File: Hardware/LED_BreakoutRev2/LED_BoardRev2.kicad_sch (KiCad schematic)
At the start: 39 parts

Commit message: First draft of LED board Schematic
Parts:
- added Conn?: Molex_SL_08, symbol MRDT_Connectors:Molex_SL_08
- added D? (x2): 365nm, symbol Device:LED
- added D? (x2): 265nm, symbol Device:LED
- added D? (x2): 275nm, symbol Device:LED
- added D? (x2): 310nm, symbol Device:LED
- added D?: LED, symbol Device:LED
- added D? (x2): 285nm, symbol Device:LED
- added Q? (x6): BSS214NW, Package_TO_SOT_SMD:SOT-323_SC-70, symbol Transistor_FET:BSS214NW
- added R? (x11): R, symbol Device:R
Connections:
- net +12V: now also Conn?.7, D?.2 (A), D?.2 (A), D?.2 (A), D?.2 (A), D?.2 (A), D?.2 (A), D?.2 (A), D?.2 (A), D?.2 (A), D?.2 (A), D?.2 (A)
- net GND: now also Conn?.8, Q?.2 (S), Q?.2 (S), Q?.2 (S), Q?.2 (S), Q?.2 (S), Q?.2 (S)
- new net: Conn?.2, Q?.1 (G)
- new net: Q?.3 (D), R?.2, R?.2 (x5)
- new net: Conn?.5, Q?.1 (G)
- new net: D?.1 (K), R?.1 (x11)
- new net: Q?.3 (D), R?.2
- new net: Conn?.1, Q?.1 (G)
- new net: Conn?.4, Q?.1 (G)
- new net: Conn?.3, Q?.1 (G)
- new net: Conn?.6, Q?.1 (G)
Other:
- moved on the sheet: Conn?, D?, Q?, R?, V?

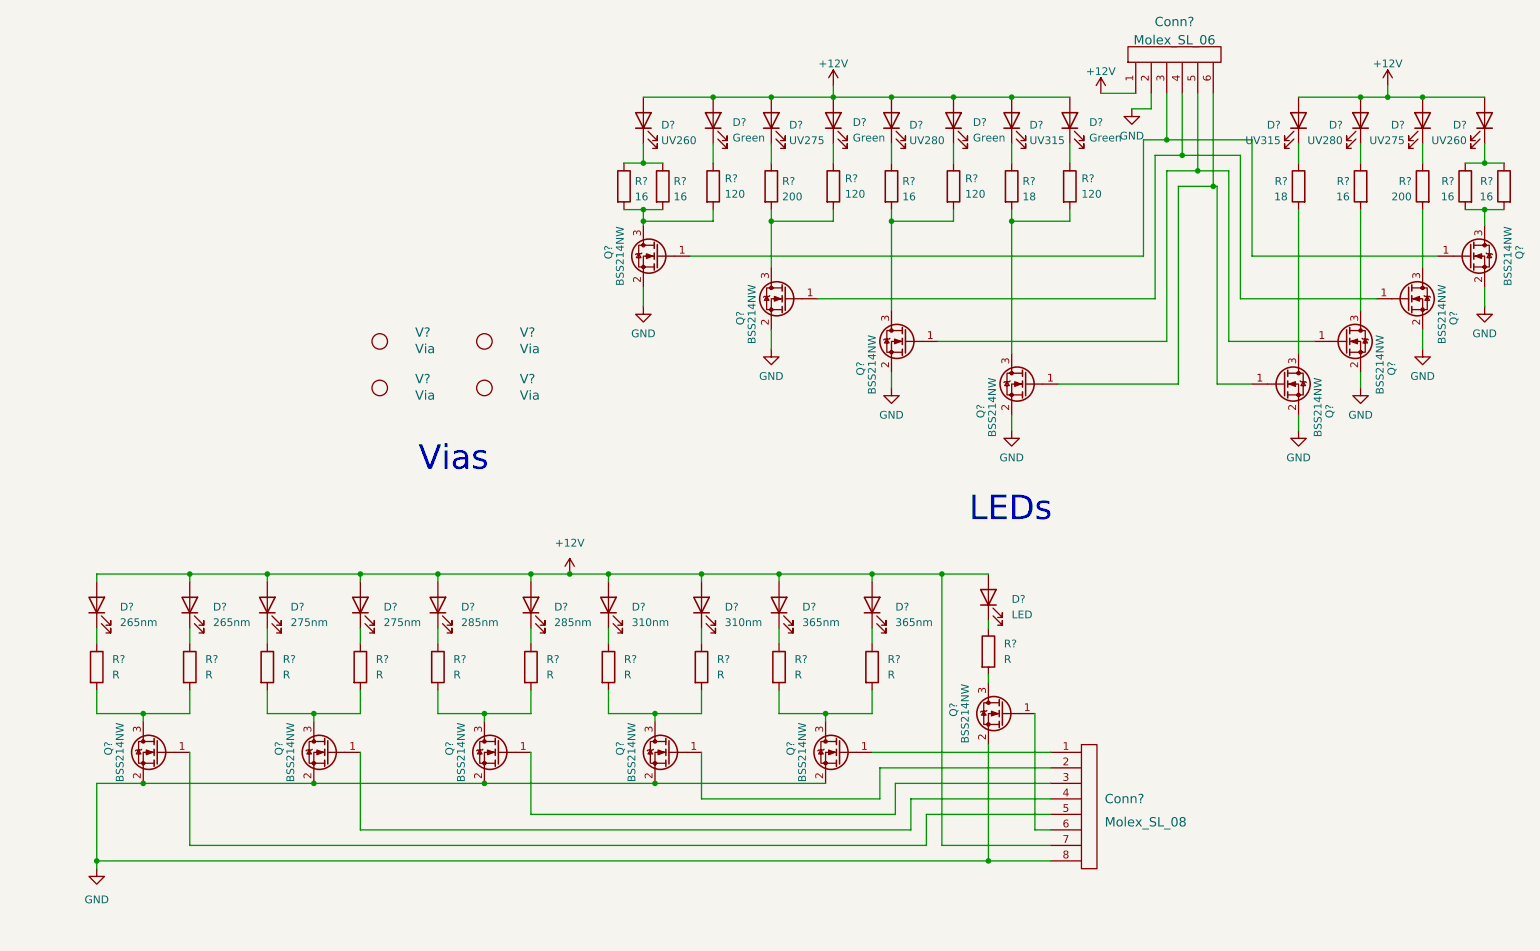
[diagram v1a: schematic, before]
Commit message: LED footprints
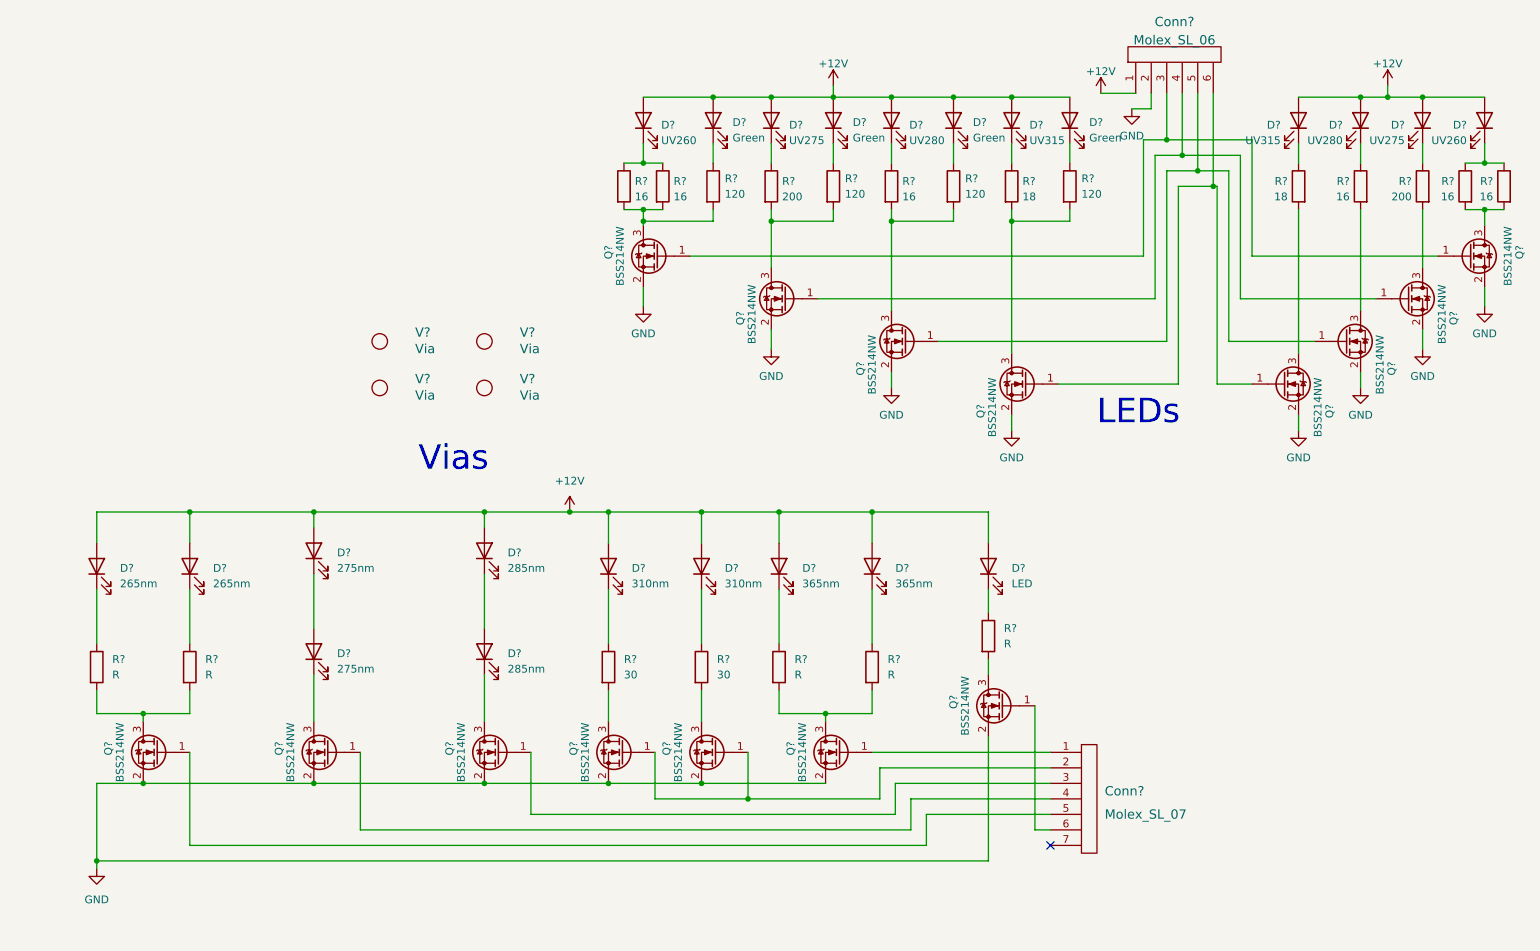
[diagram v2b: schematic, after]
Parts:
- removed Conn?: Molex_SL_08, symbol MRDT_Connectors:Molex_SL_08
- removed D? (x2): 265nm, symbol Device:LED
- removed D?: 275nm, symbol Device:LED
- removed R? (x5): R, symbol Device:R
- added Conn?: Molex_SL_07, symbol MRDT_Connectors:Molex_SL_07
- added D? (x2): 265nm, KL265-50W-SM-WD Footprint:3535, symbol Device:LED
- added D?: 275nm, symbol Device:LED
- added Q?: BSS214NW, Package_TO_SOT_SMD:SOT-323_SC-70, symbol Transistor_FET:BSS214NW
- added R?: 30, symbol Device:R
- R?: value R -> 30
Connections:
- net +12V: now also D?.2 (A), D?.2 (A), D?.2 (A); no longer D?.2 (A), D?.2 (A)
- net GND: now also Q?.2 (S)
- net at Q?.1 (G): now also Conn?.2, Q?.1 (G)
- net at Q?.3 (D): now also R?.2; no longer R?.2
- net at Q?.1 (G): now also Conn?.5
- net at D?.1 (K): now also R?.1
- net at D?.1 (K): now also Q?.3 (D) (x2)
- net at R?.1: now also D?.1 (K) (x2)
- net at Q?.1 (G): now also Conn?.1
- net at D?.1 (K): now also D?.2 (A)
- net at Q?.1 (G): now also Conn?.4
- net at Q?.1 (G): now also Conn?.3
- net at Q?.1 (G): now also Conn?.6
- new net: Q?.3 (D), R?.2
- new net: D?.1 (K), D?.2 (A)
- no-connect marks 0 -> 1
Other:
- moved on the sheet: D?, Q?, R?

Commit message: Added resistor values and LED datasheets
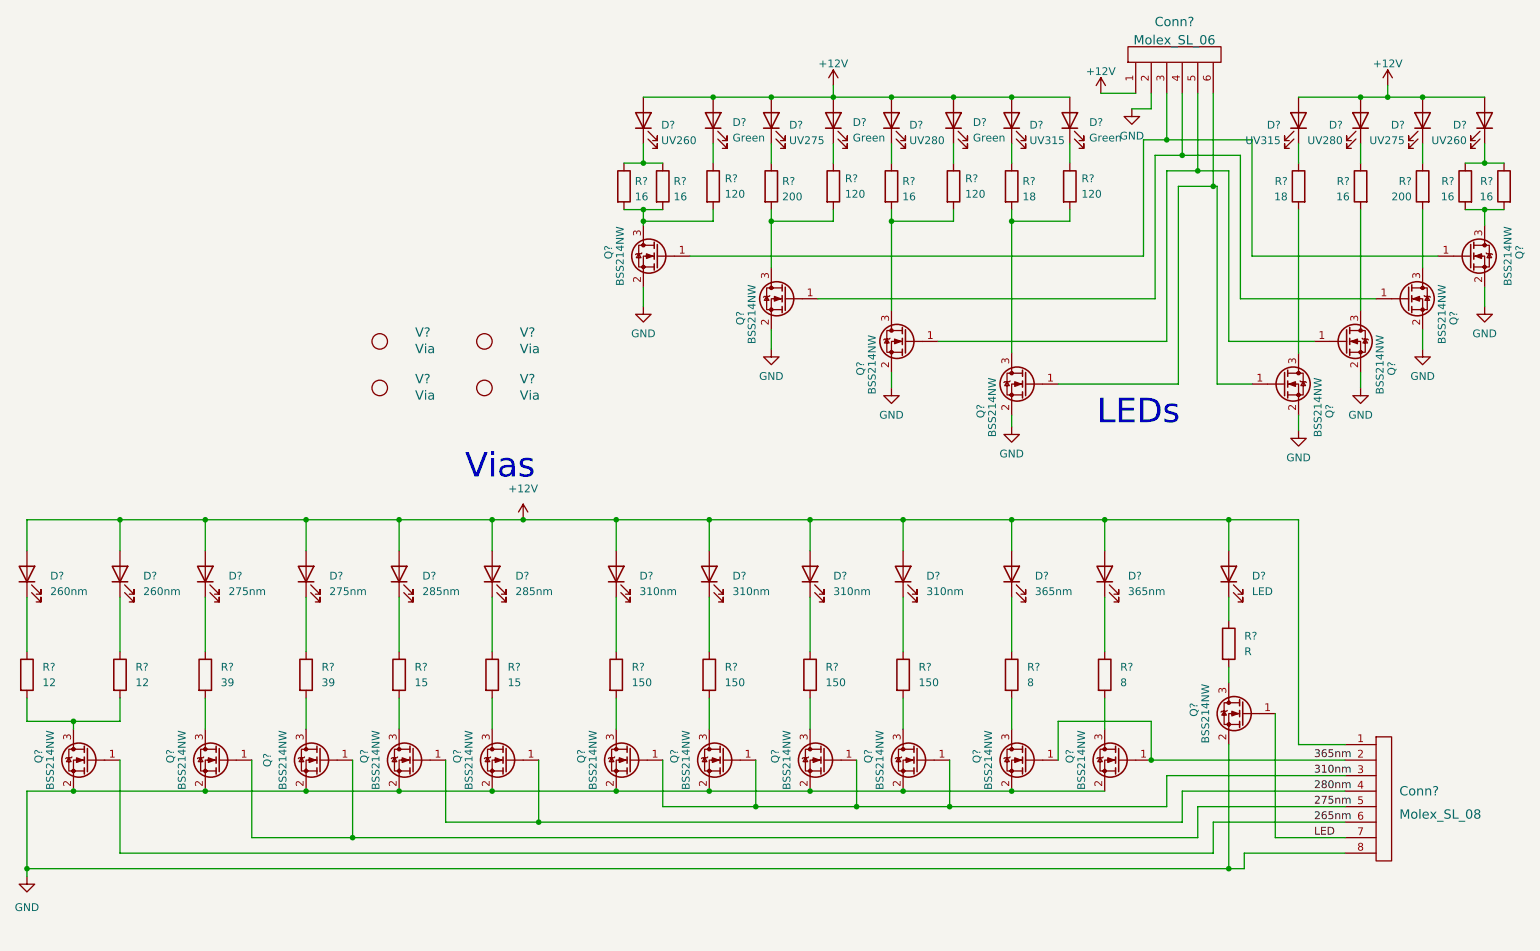
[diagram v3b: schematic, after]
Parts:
- removed Conn?: Molex_SL_07, symbol MRDT_Connectors:Molex_SL_07
- removed D?: 265nm, KL265-50W-SM-WD Footprint:3535, symbol Device:LED
- removed D?: 275nm, symbol Device:LED
- removed D?: 285nm, symbol Device:LED
- removed D?: 365nm, symbol Device:LED
- removed D?: 310nm, symbol Device:LED
- removed R? (x2): R, symbol Device:R
- removed R?: 30, symbol Device:R
- added Conn?: Molex_SL_08, symbol MRDT_Connectors:Molex_SL_08
- added D? (x3): 310nm, symbol Device:LED
- added D?: 260nm, KL265-50W-SM-WD Footprint:3535, symbol Device:LED
- added D?: 365nm, symbol Device:LED
- added D?: 285nm, symbol Device:LED
- added D?: 275nm, symbol Device:LED
- added Q? (x5): BSS214NW, Package_TO_SOT_SMD:SOT-323_SC-70, symbol Transistor_FET:BSS214NW
- added R?: 12, symbol Device:R
- added R? (x3): 150, symbol Device:R
- added R?: 8, symbol Device:R
- added R? (x2): 15, symbol Device:R
- added R? (x2): 39, symbol Device:R
- D?: value 265nm -> 260nm
- R?: value 30 -> 150
- R?: value R -> 12
- R?: value R -> 8
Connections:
- net +12V: now also D?.2 (A), D?.2 (A), Conn?.1, D?.2 (A), D?.2 (A), D?.2 (A), D?.2 (A), D?.2 (A), D?.2 (A), D?.2 (A)
- net GND: now also Conn?.8, Q?.2 (S), Q?.2 (S), Q?.2 (S), Q?.2 (S), Q?.2 (S)
- net 310nm: now reaches Q?.1 (G), Q?.1 (G)
- net 310nm: now also Conn?.3, Q?.1 (G), Q?.1 (G)
- net 265nm: now reaches Q?.1 (G)
- net 265nm: now also Conn?.6
- net at Q?.3 (D), R?.2: now also R?.2
- net at R?.2: now also Q?.3 (D); no longer Q?.3 (D)
- net at Q?.3 (D): now also R?.2
- net 365nm: now reaches Q?.1 (G)
- net 365nm: now also Conn?.2, Q?.1 (G)
- net 275nm: now reaches Q?.1 (G)
- net 275nm: now also Conn?.5, Q?.1 (G)
- net at Q?.3 (D): now also R?.2; no longer D?.1 (K)
- net 280nm: now reaches Q?.1 (G)
- net 280nm: now also Conn?.4, Q?.1 (G)
- net LED: now reaches Q?.1 (G)
- net LED: now also Conn?.7
- net at D?.1 (K): now also R?.1; no longer Q?.3 (D)
- new net: D?.1 (K), R?.1 (x8)
- new net: Q?.3 (D), R?.2 (x6)
- no-connect marks 1 -> 0
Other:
- moved on the sheet: D?, Q?, R?

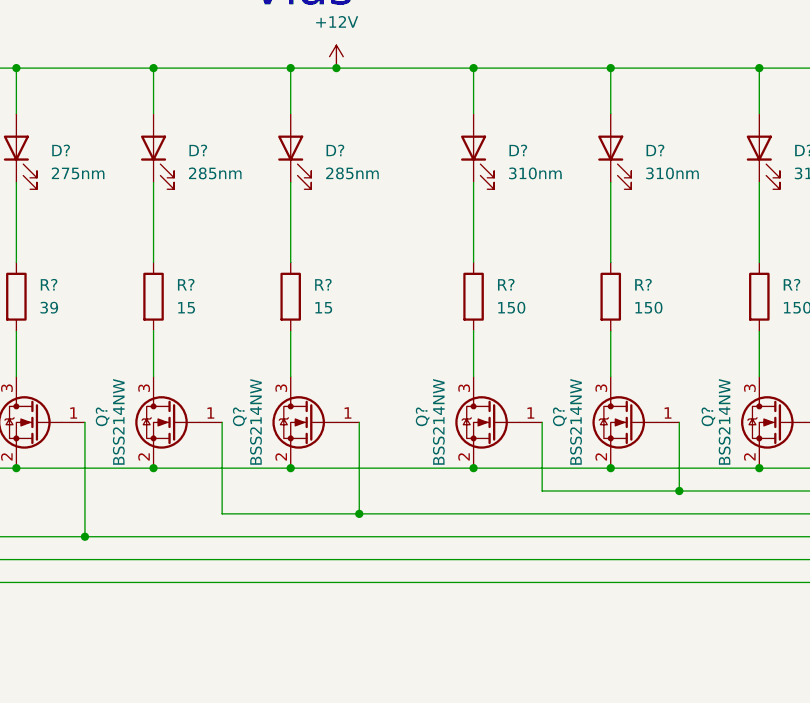
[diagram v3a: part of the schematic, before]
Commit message: More Footprints
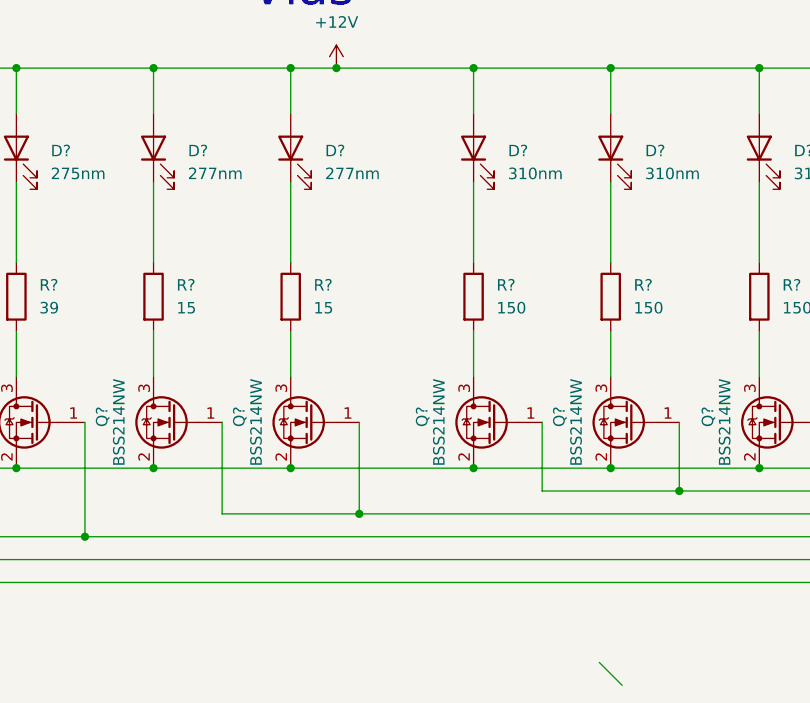
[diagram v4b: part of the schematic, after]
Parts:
- removed D? (x3): 310nm, symbol Device:LED
- removed D?: 285nm, symbol Device:LED
- removed D?: 275nm, symbol Device:LED
- added D?: 277nm, MRDT_Devices:280nm, symbol Device:LED
- added D?: 275nm, MRDT_Devices:275nm LED, symbol Device:LED
- added D? (x3): 310nm, MRDT_Devices:310nm, symbol Device:LED
- D?: footprint (none) -> MRDT_Devices:275nm LED
- D?: footprint (none) -> MRDT_Devices:310nm
- D?: value 285nm -> 277nm; footprint (none) -> MRDT_Devices:280nm
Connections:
- net +12V: now also D?.2 (A), D?.2 (A), D?.2 (A), D?.2 (A), D?.2 (A)
- net at R?.1: now also D?.1 (K) (x5)

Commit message: re-arranged schematic
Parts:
- removed Conn?: Molex_SL_06, UVLEDs:705550040, symbol Molex_SL_06:Molex_SL_06
- removed Conn?: Molex_SL_08, symbol MRDT_Connectors:Molex_SL_08
- removed D? (x2): UV275, UVLEDs:SUCULBN1VCAGAY674F4G30R18, symbol Device:LED
- removed D? (x2): UV315, UVLEDs:WS3535C48LF-310, symbol Device:LED
- removed D? (x4): Green, LED_SMD:LED_0603_1608Metric_Pad1.05x0.95mm_HandSolder, symbol Device:LED
- removed D? (x2): UV260, UVLEDs:KL26550USMWD, symbol Device:LED
- removed D?: LED, symbol Device:LED
- removed D? (x2): UV280, UVLEDs:XBT3535UVA130CD27501, symbol Device:LED
- removed Q? (x9): BSS214NW, Package_TO_SOT_SMD:SOT-323_SC-70, symbol Transistor_FET:BSS214NW
- removed R? (x2): 200, Resistor_SMD:R_0603_1608Metric_Pad0.98x0.95mm_HandSolder, symbol Device:R
- removed R? (x2): 18, Resistor_SMD:R_2512_6332Metric_Pad1.40x3.35mm_HandSolder, symbol Device:R
- removed R? (x4): 120, Resistor_SMD:R_0603_1608Metric_Pad0.98x0.95mm_HandSolder, symbol Device:R
- removed R?: R, symbol Device:R
- removed R? (x6): 16, Resistor_SMD:R_2512_6332Metric_Pad1.40x3.35mm_HandSolder, symbol Device:R
- removed V? (x4): Via, MRDT_Drill_Holes:4_40_Hole, symbol MRDT_Drill_Holes:Via
- added Conn?: Molex_SL_07, symbol MRDT_Connectors:Molex_SL_07
- added SW? (x8): SW_MEC_5G, symbol Switch:SW_MEC_5G
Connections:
- net +12V: now also Conn?.1
- net 275nm: now also Conn?.5
- net 280nm: now also Conn?.4
- net 310nm: now also Conn?.3
- net 365nm: now also Conn?.2
- net GND: now also Conn?.7, SW?.1 (A), SW?.1 (A), SW?.1 (A), SW?.1 (A), SW?.1 (A), SW?.1 (A), SW?.1 (A), SW?.1 (A), SW?.2 (A), SW?.2 (A), SW?.2 (A), SW?.2 (A), SW?.2 (A), SW?.2 (A), SW?.2 (A), SW?.2 (A)
- net at Q?.3 (D), R?.2: now also SW?.3 (B), SW?.4 (B) (x7)
- net at Q?.3 (D), R?.2: now also Q?.3 (D), R?.2, SW?.3 (B), SW?.4 (B)
- net 265nm renamed 260nm
- net 260nm: now also Conn?.6
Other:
- note removed: "LEDs"
- note removed: "Vias"
- moved on the sheet: D?, Q?, R?
